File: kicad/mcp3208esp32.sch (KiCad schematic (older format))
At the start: 25 parts, among them J1 Conn_01x04, J2 Conn_01x04, J3 Conn_01x04, U1 LM324, U2 LM324

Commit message: Modified the source of the voltage reference
Now it uses the input voltage in contrast to before when the regulated 5V was the source for the reference voltage. This is an improvement because now the board can use 5V or 2.5V reference.
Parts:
- AIA1, AIB1, AIC1, AID1, AIGND1: value Conn_01x02_MountingPin -> Conn_01x02; symbol Connector_Generic_MountingPin:Conn_01x02_MountingPin -> Connector_Generic:Conn_01x02
- ESPLEFT1, ESPRIGHT1, HDRLEFT1, HDRRIGHT1: value Conn_01x20_MountingPin -> Conn_01x20; symbol Connector_Generic_MountingPin:Conn_01x20_MountingPin -> Connector_Generic:Conn_01x20
- HDRADC1: symbol Connector_Generic_MountingPin:Conn_01x04_MountingPin -> Connector_Generic:Conn_01x04
- VIN1: value Conn_01x04_MountingPin -> Conn_01x04; symbol Connector_Generic_MountingPin:Conn_01x04_MountingPin -> Connector_Generic:Conn_01x04
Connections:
- net at 5V1.3 (VO), ADC1.16 (Vdd), COUT1.1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: no longer Rref1.2
- net at 5V1.1 (VI), CPIN1.1, J1.1 (Pin_1)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: now also Rref1.2
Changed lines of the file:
@@
 $EndDescr
 $Comp
-L Connector_Generic_MountingPin:Conn_01x20_MountingPin ESPLEFT1
+L Connector_Generic:Conn_01x20 ESPLEFT1
 U 1 1 5F79C20C
 P 2450 2400
 F 0 "ESPLEFT1" V 2675 2268 50  0000 C CNN
-F 1 "Conn_01x20_MountingPin" V 2584 2268 50  0000 C CNN
+F 1 "Conn_01x20" V 2584 2268 50  0000 C CNN
 F 2 "Connector_PinSocket_2.54mm:PinSocket_1x20_P2.54mm_Vertical" H 2450 2400 50  0001 C CNN
 F 3 "~" H 2450 2400 50  0001 C CNN
@@
 $EndComp
 $Comp
-L Connector_Generic_MountingPin:Conn_01x20_MountingPin HDRLEFT1
+L Connector_Generic:Conn_01x20 HDRLEFT1
 U 1 1 5F79DBF9
 P 2450 1950
 F 0 "HDRLEFT1" V 2675 1818 50  0000 C CNN
-F 1 "Conn_01x20_MountingPin" V 2584 1818 50  0000 C CNN
+F 1 "Conn_01x20" V 2584 1818 50  0000 C CNN
 F 2 "Connector_PinHeader_2.54mm:PinHeader_1x20_P2.54mm_Vertical" H 2450 1950 50  0001 C CNN
 F 3 "~" H 2450 1950 50  0001 C CNN
@@
 $EndComp
 $Comp
-L Connector_Generic_MountingPin:Conn_01x20_MountingPin ESPRIGHT1
+L Connector_Generic:Conn_01x20 ESPRIGHT1
 U 1 1 5F79F80C
 P 2450 3650
 F 0 "ESPRIGHT1" V 2675 3518 50  0000 C CNN
-F 1 "Conn_01x20_MountingPin" V 2584 3518 50  0000 C CNN
+F 1 "Conn_01x20" V 2584 3518 50  0000 C CNN
 F 2 "Connector_PinSocket_2.54mm:PinSocket_1x20_P2.54mm_Vertical" H 2450 3650 50  0001 C CNN
 F 3 "~" H 2450 3650 50  0001 C CNN
@@
 $EndComp
 $Comp
-L Connector_Generic_MountingPin:Conn_01x20_MountingPin HDRRIGHT1
+L Connector_Generic:Conn_01x20 HDRRIGHT1
 U 1 1 5F7A039E
 P 2450 4200
 F 0 "HDRRIGHT1" V 2675 4068 50  0000 C CNN
-F 1 "Conn_01x20_MountingPin" V 2584 4068 50  0000 C CNN
+F 1 "Conn_01x20" V 2584 4068 50  0000 C CNN
 F 2 "Connector_PinHeader_2.54mm:PinHeader_1x20_P2.54mm_Vertical" H 2450 4200 50  0001 C CNN
 F 3 "~" H 2450 4200 50  0001 C CNN
@@
 $EndComp
 $Comp
-L Connector_Generic_MountingPin:Conn_01x04_MountingPin HDRADC1
+L Connector_Generic:Conn_01x04 HDRADC1
 U 1 1 5F7B7F43
 P 4850 3100
@@
 	4650 3300 5200 3300
 $Comp
-L Connector_Generic_MountingPin:Conn_01x04_MountingPin VIN1
+L Connector_Generic:Conn_01x04 VIN1
 U 1 1 5F7BFE67
 P 4600 1550
 F 0 "VIN1" V 4825 1418 50  0000 C CNN
-F 1 "Conn_01x04_MountingPin" V 4734 1418 50  0000 C CNN
+F 1 "Conn_01x04" V 4734 1418 50  0000 C CNN
 F 2 "TerminalBlock:TerminalBlock_bornier-4_P5.08mm" H 4600 1550 50  0001 C CNN
 F 3 "~" H 4600 1550 50  0001 C CNN
@@
 Wire Wire Line
 	6100 1750 6150 1750
-Wire Wire Line
-	6650 1750 6650 4000
 Wire Wire Line
 	6650 4000 5600 4000
@@
 Wire Wire Line
 	6650 1750 6750 1750
-Connection ~ 6650 1750
 Wire Wire Line
 	7450 1800 7300 1800
@@
 Wire Wire Line
 	6450 700  6950 700
-Connection ~ 6450 1750
-Wire Wire Line
-	6450 1750 6650 1750
 Wire Wire Line
 	6950 700  7400 700
@@
 	8750 3200 6400 3200
 $Comp
-L Connector_Generic_MountingPin:Conn_01x02_MountingPin AID1
+L Connector_Generic:Conn_01x02 AID1
 U 1 1 5F8BB3AE
 P 10100 2000
 F 0 "AID1" H 10188 1914 50  0000 L CNN
-F 1 "Conn_01x02_MountingPin" H 10188 1823 50  0000 L CNN
+F 1 "Conn_01x02" H 10188 1823 50  0000 L CNN
 F 2 "TerminalBlock:TerminalBlock_bornier-2_P5.08mm" H 10100 2000 50  0001 C CNN
 F 3 "~" H 10100 2000 50  0001 C CNN
@@
 $EndComp
 $Comp
-L Connector_Generic_MountingPin:Conn_01x02_MountingPin AIC1
+L Connector_Generic:Conn_01x02 AIC1
 U 1 1 5F8BBE73
 P 10100 2350
 F 0 "AIC1" H 10188 2264 50  0000 L CNN
-F 1 "Conn_01x02_MountingPin" H 10188 2173 50  0000 L CNN
+F 1 "Conn_01x02" H 10188 2173 50  0000 L CNN
 F 2 "TerminalBlock:TerminalBlock_bornier-2_P5.08mm" H 10100 2350 50  0001 C CNN
 F 3 "~" H 10100 2350 50  0001 C CNN
@@
 $EndComp
 $Comp
-L Connector_Generic_MountingPin:Conn_01x02_MountingPin AIB1
+L Connector_Generic:Conn_01x02 AIB1
 U 1 1 5F8BC796
 P 10100 2750
 F 0 "AIB1" H 10188 2664 50  0000 L CNN
-F 1 "Conn_01x02_MountingPin" H 10188 2573 50  0000 L CNN
+F 1 "Conn_01x02" H 10188 2573 50  0000 L CNN
 F 2 "TerminalBlock:TerminalBlock_bornier-2_P5.08mm" H 10100 2750 50  0001 C CNN
 F 3 "~" H 10100 2750 50  0001 C CNN
@@
 $EndComp
 $Comp
-L Connector_Generic_MountingPin:Conn_01x02_MountingPin AIA1
+L Connector_Generic:Conn_01x02 AIA1
 U 1 1 5F8BD07B
 P 10100 3150
 F 0 "AIA1" H 10188 3064 50  0000 L CNN
-F 1 "Conn_01x02_MountingPin" H 10188 2973 50  0000 L CNN
+F 1 "Conn_01x02" H 10188 2973 50  0000 L CNN
 F 2 "TerminalBlock:TerminalBlock_bornier-2_P5.08mm" H 10100 3150 50  0001 C CNN
 F 3 "~" H 10100 3150 50  0001 C CNN
@@
 	1    0    0    -1
 $EndComp
-$Comp
-L Connector_Generic_MountingPin:Conn_01x02_MountingPin AIGND1
-U 1 1 5F8BD987
-P 4550 4650
-F 0 "AIGND1" H 4638 4564 50  0000 L CNN
-F 1 "Conn_01x02_MountingPin" H 4638 4473 50  0000 L CNN
-F 2 "TerminalBlock:TerminalBlock_bornier-2_P5.08mm" H 4550 4650 50  0001 C CNN
-F 3 "~" H 4550 4650 50  0001 C CNN
-	1    4550 4650
-	1    0    0    -1
-$EndComp
 Wire Wire Line
 	9900 2000 9700 2000
@@
 	9650 4850 9350 4850
 Wire Wire Line
-	4350 4750 4350 4650
-Wire Wire Line
-	4350 4650 4350 2050
-Wire Wire Line
 	4350 2050 4500 2050
-Connection ~ 4350 4650
 Connection ~ 4500 2050
 Wire Wire Line
@@
 Connection ~ 6150 1450
 Wire Wire Line
-	5100 1200 5100 1750
+	5100 1200 5100 1350
 Wire Wire Line
 	4200 1750 4200 2050
@@
 Wire Wire Line
 	5900 2050 6100 2050
+Wire Wire Line
+	6650 1750 6650 1000
+Wire Wire Line
+	6650 1000 5250 1000
+Wire Wire Line
+	5250 1000 5250 1350
+Wire Wire Line
+	5250 1350 5100 1350
+Connection ~ 5100 1350
+Wire Wire Line
+	5100 1350 5100 1750
+Wire Wire Line
+	4350 4650 4350 2050
+Wire Wire Line
+	4350 4750 4350 4650
+Connection ~ 4350 4650
+$Comp
+L Connector_Generic:Conn_01x02 AIGND1
+U 1 1 5F8BD987
+P 4550 4650
+F 0 "AIGND1" H 4638 4564 50  0000 L CNN
+F 1 "Conn_01x02" H 4638 4473 50  0000 L CNN
+F 2 "TerminalBlock:TerminalBlock_bornier-2_P5.08mm" H 4550 4650 50  0001 C CNN
+F 3 "~" H 4550 4650 50  0001 C CNN
+	1    4550 4650
+	1    0    0    -1
+$EndComp
+Wire Wire Line
+	6650 4000 6650 2100
+Wire Wire Line
+	6650 2100 6450 2100
+Wire Wire Line
+	6450 2100 6450 1750
+Connection ~ 6450 1750
 $EndSCHEMATC

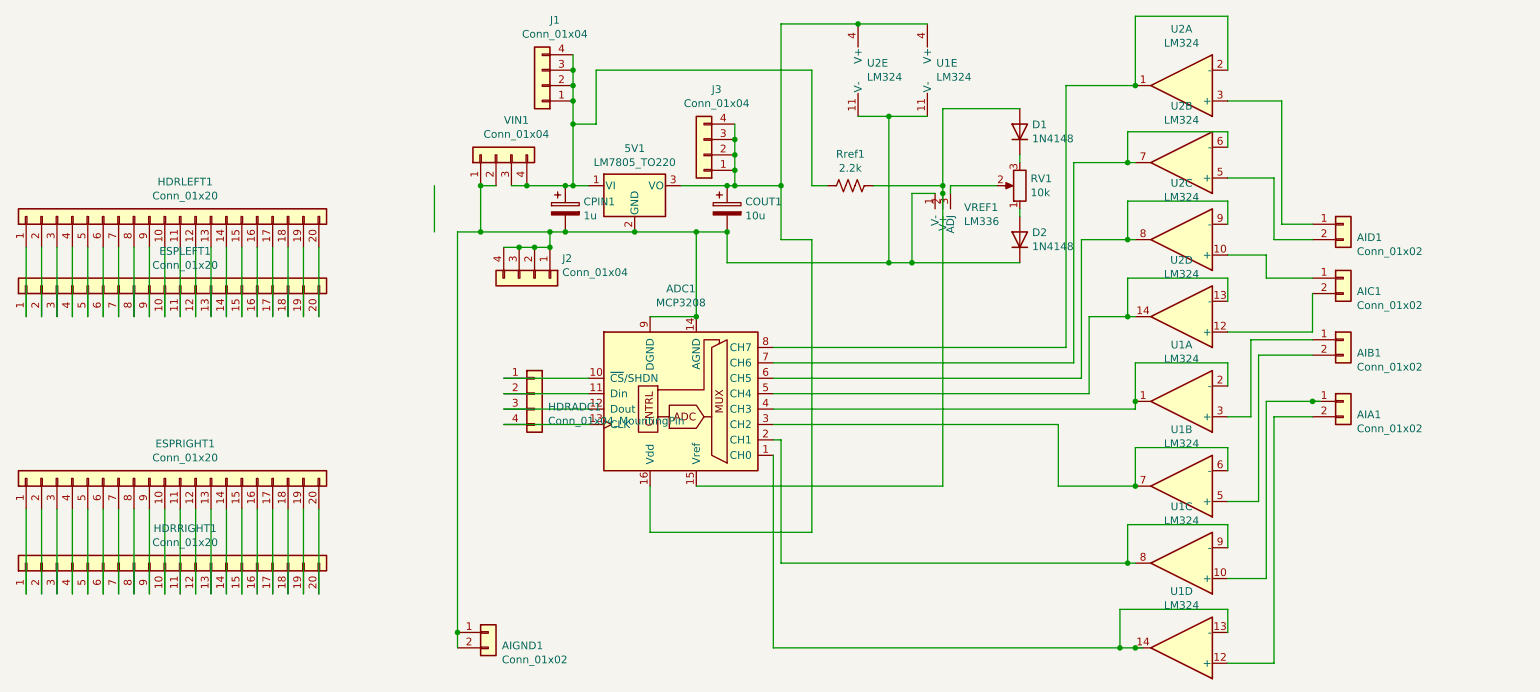
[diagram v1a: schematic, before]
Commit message: Removed the operational amplifier
It was not working and not helping. So for now I removed it.

I also added a header connector that exposes the reference voltage to other applications.
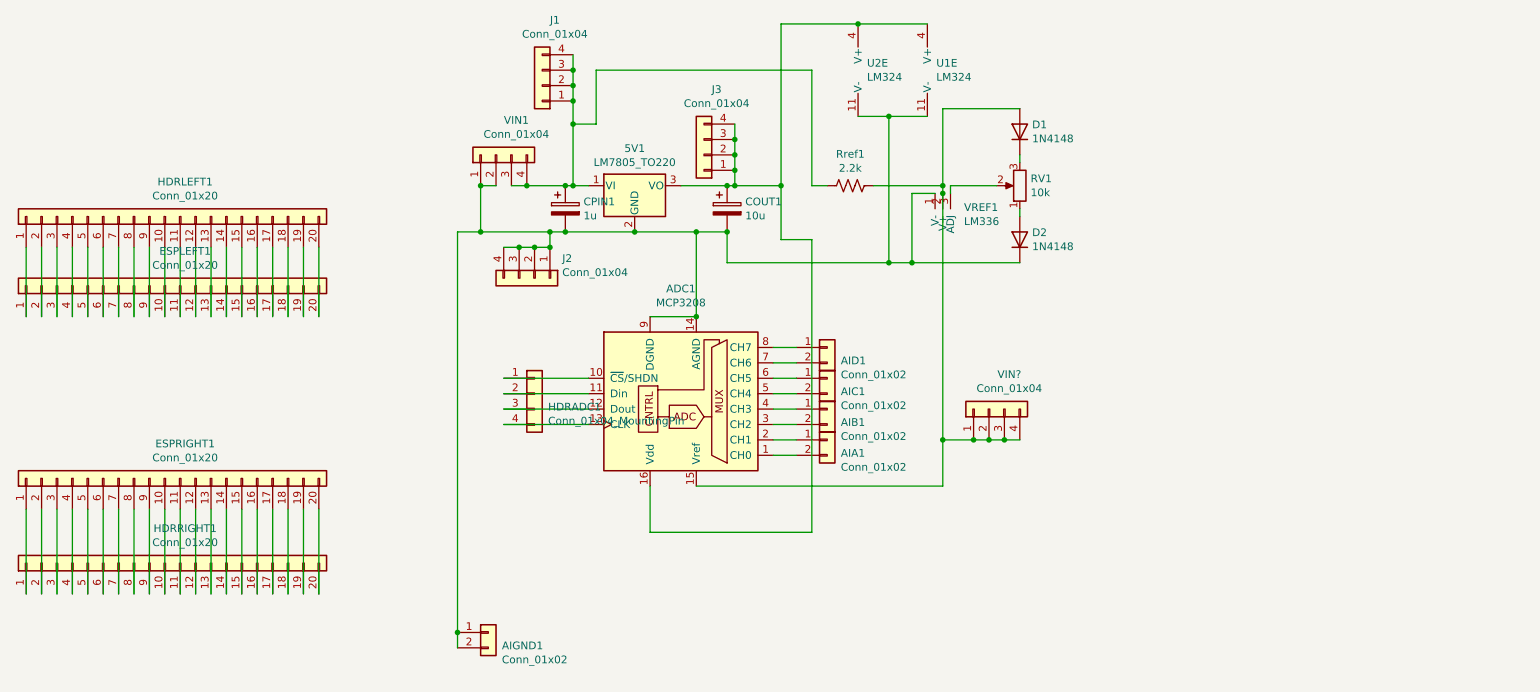
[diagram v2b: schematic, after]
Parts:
- removed unit 1 of U1
- removed unit 2 of U1
- removed unit 3 of U1
- removed unit 4 of U1
- removed unit 1 of U2
- removed unit 2 of U2
- removed unit 3 of U2
- removed unit 4 of U2
- added VIN?: Conn_01x04, TerminalBlock:TerminalBlock_bornier-4_P5.08mm, symbol Connector_Generic:Conn_01x04
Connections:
- net at ADC1.1 (CH0): now also AIA1.2 (Pin_2)
- net at ADC1.15 (Vref), D1.2 (A), Rref1.1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: now also VIN?.1 (Pin_1), VIN?.2 (Pin_2), VIN?.3 (Pin_3), VIN?.4 (Pin_4)
- net at ADC1.2 (CH1): now also AIA1.1 (Pin_1)
- net at ADC1.3 (CH2): now also AIB1.2 (Pin_2)
- net at ADC1.4 (CH3): now also AIB1.1 (Pin_1)
- net at ADC1.5 (CH4): now also AIC1.2 (Pin_2)
- net at ADC1.6 (CH5): now also AIC1.1 (Pin_1)
- net at ADC1.7 (CH6): now also AID1.2 (Pin_2)
- net at ADC1.8 (CH7): now also AID1.1 (Pin_1)
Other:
- moved on the sheet: AIA1, AIB1, AIC1, AID1

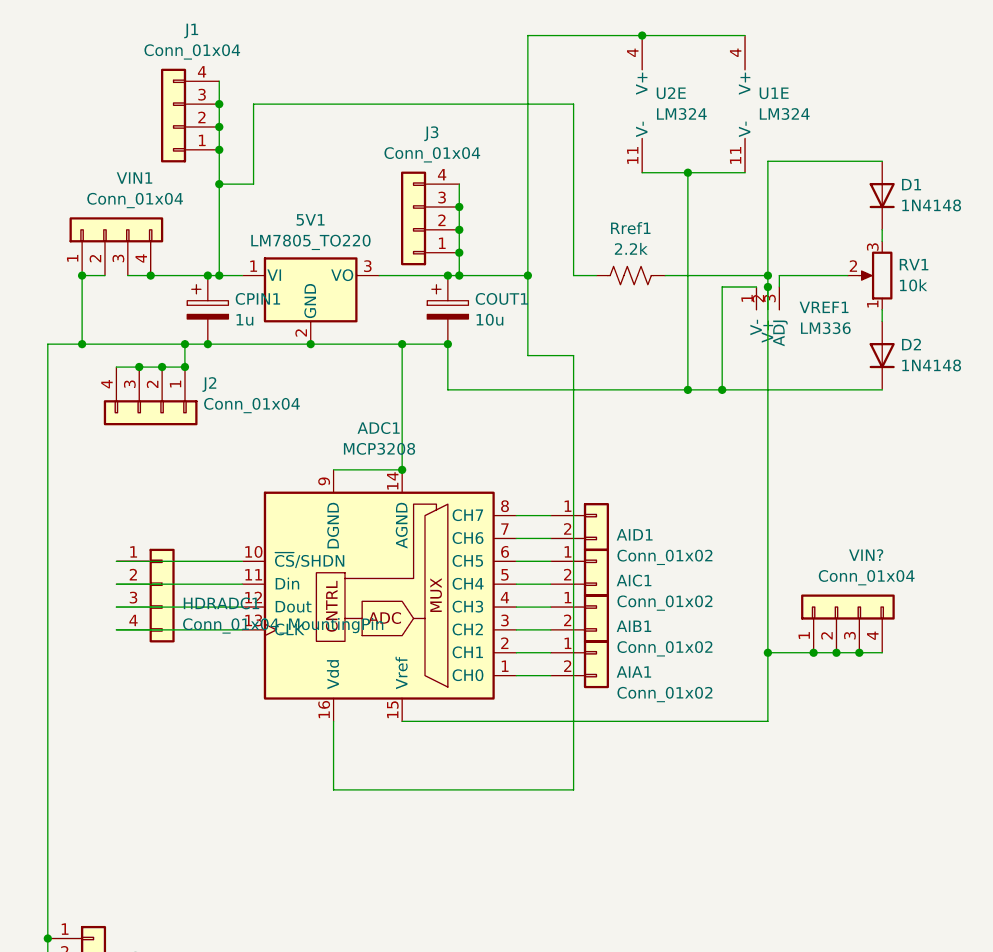
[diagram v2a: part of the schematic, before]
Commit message: Updated the pcb without the op amps
AGND and DGND are connected. Any signal conditioning will have to be done upstream.
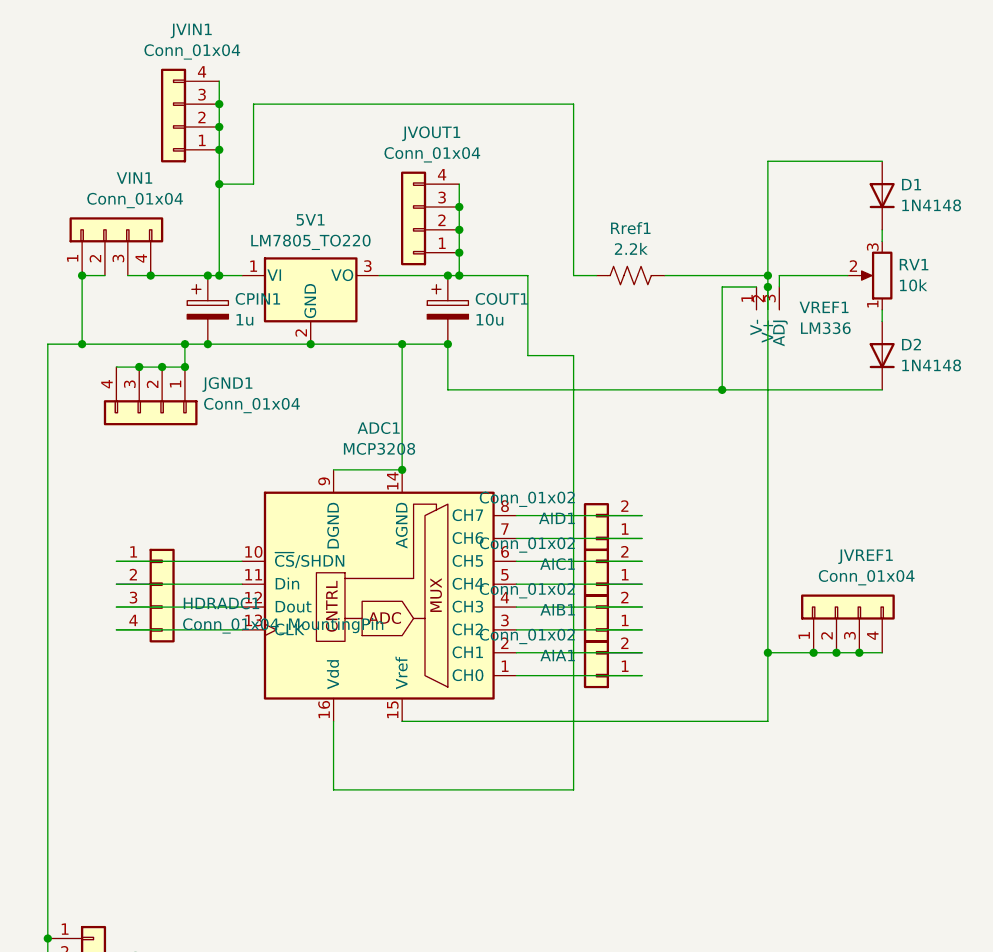
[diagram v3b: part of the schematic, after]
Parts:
- removed U1, U2: LM324, Package_DIP:DIP-14_W7.62mm, symbol Amplifier_Operational:LM324
- JVREF1: renamed from VIN?; footprint TerminalBlock:TerminalBlock_bornier-4_P5.08mm -> Connector_PinHeader_2.54mm:PinHeader_1x04_P2.54mm_Vertical
- renumbered J2 to JGND1, J1 to JVIN1, J3 to JVOUT1
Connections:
- net at ADC1.1 (CH0): now also AIA1.1 (Pin_1); no longer AIA1.2 (Pin_2)
- net at ADC1.2 (CH1): now also AIA1.2 (Pin_2); no longer AIA1.1 (Pin_1)
- net at ADC1.3 (CH2): now also AIB1.1 (Pin_1); no longer AIB1.2 (Pin_2)
- net at ADC1.4 (CH3): now also AIB1.2 (Pin_2); no longer AIB1.1 (Pin_1)
- net at ADC1.5 (CH4): now also AIC1.1 (Pin_1); no longer AIC1.2 (Pin_2)
- net at ADC1.6 (CH5): now also AIC1.2 (Pin_2); no longer AIC1.1 (Pin_1)
- net at ADC1.7 (CH6): now also AID1.1 (Pin_1); no longer AID1.2 (Pin_2)
- net at ADC1.8 (CH7): now also AID1.2 (Pin_2); no longer AID1.1 (Pin_1)
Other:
- moved on the sheet: AIA1, AIB1, AIC1, AID1
